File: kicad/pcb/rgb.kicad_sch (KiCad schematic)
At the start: 13 parts

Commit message: getting ready for prototype
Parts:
- removed JP1: Jumper_2_Open, Jumper:SolderJumper-2_P1.3mm_Open_TrianglePad1.0x1.5mm, symbol Jumper:Jumper_2_Open
- added JP2: SolderJumper_3_Open, Jumper:SolderJumper-3_P1.3mm_Open_RoundedPad1.0x1.5mm, symbol Jumper:SolderJumper_3_Open
- D101, D102, D103, D104, D105, D106, D107, D108, D109, D110, D111: footprint modified_footrprints:LED_SK6812MINI_PLCC4_3.5x3.5mm_P1.75mm -> modified_footprints:LED_SK6812MINI_PLCC4_3.5x3.5mm_P1.75mm
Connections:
- net RGB: now also JP2.2 (C)
- net at D111.3 (DIN), J?.2 (Pin_2): now also JP2.3 (B)
- net at D102.1 (DOUT), D103.3 (DIN): now also JP2.1 (A)
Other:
- title: Hotswap Chiffre -> Le Capybara
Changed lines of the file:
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@@
   (paper "A4")
   (title_block
-    (title "Hotswap Chiffre")
-    (date "2023-07-07")
-    (rev "0.2")
+    (title "Le Capybara")
+    (date "2023-08-22")
+    (rev "0.1")
     (company "sporkus")
   )
@@
   (junction (at 136.525 69.215) (diameter 0) (color 0 0 0 0)
   )
+  (junction (at 82.801 89.535) (diameter 0) (color 0 0 0 0)
+  )
   (junction (at 100.965 53.975) (diameter 0) (color 0 0 0 0)
   )
+  (junction (at 67.31 50.8) (diameter 0) (color 0 0 0 0)
+  )
   (junction (at 154.305 53.975) (diameter 0) (color 0 0 0 0)
   )
@@
   (junction (at 111.125 81.915) (diameter 0) (color 0 0 0 0)
   )
-  (junction (at 81.661 41.021) (diameter 0) (color 0 0 0 0)
-  )
   (junction (at 100.965 69.215) (diameter 0) (color 0 0 0 0)
   )
   (junction (at 118.745 53.975) (diameter 0) (color 0 0 0 0)
   )
+  (wire (pts (xy 64.77 50.8) (xy 67.31 50.8))
+    (stroke (width 0) (type default))
+  )
   (wire (pts (xy 78.105 84.455) (xy 78.105 86.995))
     (stroke (width 0) (type default))
@@
     (stroke (width 0) (type default))
   )
-  (wire (pts (xy 78.105 89.535) (xy 85.725 89.535))
+  (wire (pts (xy 78.105 89.535) (xy 82.801 89.535))
     (stroke (width 0) (type default))
   )
@@
     (stroke (width 0) (type default))
   )
+  (wire (pts (xy 82.801 89.535) (xy 85.725 89.535))
+    (stroke (width 0) (type default))
+  )
   (wire (pts (xy 146.685 97.155) (xy 164.465 97.155))
     (stroke (width 0) (type default))
   )
-  (wire (pts (xy 81.661 41.021) (xy 83.566 41.021))
-    (stroke (width 0) (type default))
-  )
   (wire (pts (xy 136.525 69.215) (xy 154.305 69.215))
     (stroke (width 0) (type default))
@@
     (stroke (width 0) (type default))
   )
-  (wire (pts (xy 81.661 41.021) (xy 81.661 61.595))
-    (stroke (width 0) (type default))
-  )
   (wire (pts (xy 93.345 97.155) (xy 111.125 97.155))
     (stroke (width 0) (type default))
   )
+  (wire (pts (xy 71.12 45.72) (xy 71.12 41.021))
+    (stroke (width 0) (type default))
+  )
+  (wire (pts (xy 71.12 68.58) (xy 82.801 68.58))
+    (stroke (width 0) (type default))
+  )
+  (wire (pts (xy 81.661 50.8) (xy 81.661 61.595))
+    (stroke (width 0) (type default))
+  )
   (wire (pts (xy 111.125 97.155) (xy 128.905 97.155))
     (stroke (width 0) (type default))
   )
-  (wire (pts (xy 71.755 41.021) (xy 81.661 41.021))
+  (wire (pts (xy 67.31 50.8) (xy 81.661 50.8))
     (stroke (width 0) (type default))
   )
@@
     (stroke (width 0) (type default))
   )
-  (wire (pts (xy 93.726 41.021) (xy 127.635 41.021))
+  (wire (pts (xy 71.12 55.88) (xy 71.12 68.58))
+    (stroke (width 0) (type default))
+  )
+  (wire (pts (xy 71.12 41.021) (xy 127.635 41.021))
+    (stroke (width 0) (type default))
+  )
+  (wire (pts (xy 82.801 68.58) (xy 82.801 89.535))
     (stroke (width 0) (type default))
   )
@@
     (stroke (width 0) (type default))
   )
-  (global_label "RGB" (shape input) (at 71.755 41.021 180)
+  (global_label "RGB" (shape input) (at 64.77 50.8 180)
     (effects (font (size 1.27 1.27)) (justify right))
-    (property "Intersheetrefs" "${INTERSHEET_REFS}" (at 71.755 41.021 0)
+    (property "Intersheetrefs" "${INTERSHEET_REFS}" (at 64.77 50.8 0)
       (effects (font (size 1.27 1.27)) hide)
     )
@@
       (effects (font (size 0.8 0.8)))
     )
-    (property "Footprint" "modified_footrprints:LED_SK6812MINI_PLCC4_3.5x3.5mm_P1.75mm" (at 147.955 97.155 0)
+    (property "Footprint" "modified_footprints:LED_SK6812MINI_PLCC4_3.5x3.5mm_P1.75mm" (at 147.955 97.155 0)
       (effects (font (size 1.27 1.27)) (justify left top) hide)
     )
@@
       (effects (font (size 0.8 0.8)))
     )
-    (property "Footprint" "modified_footrprints:LED_SK6812MINI_PLCC4_3.5x3.5mm_P1.75mm" (at 137.795 69.215 0)
+    (property "Footprint" "modified_footprints:LED_SK6812MINI_PLCC4_3.5x3.5mm_P1.75mm" (at 137.795 69.215 0)
       (effects (font (size 1.27 1.27)) (justify left top) hide)
     )
@@
         (path "/ca0d59d2-7f9b-4344-99bc-39bc2c8c88cb/ddb59433-fe5b-4efc-b099-e8e1feecfd95"
           (reference "D103") (unit 1)
+        )
+      )
+    )
+  )
+  (symbol (lib_id "Jumper:SolderJumper_3_Open") (at 71.12 50.8 270) (unit 1)
+    (in_bom yes) (on_board yes) (dnp no)
+    (property "Reference" "JP2" (at 73.66 53.34 90)
+      (effects (font (size 1.27 1.27)) (justify left))
+    )
+    (property "Value" "SolderJumper_3_Open" (at 46.99 57.15 90)
+      (effects (font (size 1.27 1.27)) (justify left) hide)
+    )
+    (property "Footprint" "Jumper:SolderJumper-3_P1.3mm_Open_RoundedPad1.0x1.5mm" (at 71.12 50.8 0)
+      (effects (font (size 1.27 1.27)) hide)
+    )
+    (property "Datasheet" "~" (at 71.12 50.8 0)
+      (effects (font (size 1.27 1.27)) hide)
+    )
+    (pin "1")
+    (pin "2")
+    (pin "3")
+    (instances
+      (project "le_capybara"
+        (path "/ca0d59d2-7f9b-4344-99bc-39bc2c8c88cb/ddb59433-fe5b-4efc-b099-e8e1feecfd95"
+          (reference "JP2") (unit 1)
         )
       )
@@
       (effects (font (size 0.8 0.8)))
     )
-    (property "Footprint" "modified_footrprints:LED_SK6812MINI_PLCC4_3.5x3.5mm_P1.75mm" (at 155.575 69.215 0)
+    (property "Footprint" "modified_footprints:LED_SK6812MINI_PLCC4_3.5x3.5mm_P1.75mm" (at 155.575 69.215 0)
       (effects (font (size 1.27 1.27)) (justify left top) hide)
     )
@@
       (effects (font (size 0.8 0.8)))
     )
-    (property "Footprint" "modified_footrprints:LED_SK6812MINI_PLCC4_3.5x3.5mm_P1.75mm" (at 94.615 97.155 0)
+    (property "Footprint" "modified_footprints:LED_SK6812MINI_PLCC4_3.5x3.5mm_P1.75mm" (at 94.615 97.155 0)
       (effects (font (size 1.27 1.27)) (justify left top) hide)
     )
@@
       (effects (font (size 0.8 0.8)))
     )
-    (property "Footprint" "modified_footrprints:LED_SK6812MINI_PLCC4_3.5x3.5mm_P1.75mm" (at 165.735 97.155 0)
+    (property "Footprint" "modified_footprints:LED_SK6812MINI_PLCC4_3.5x3.5mm_P1.75mm" (at 165.735 97.155 0)
       (effects (font (size 1.27 1.27)) (justify left top) hide)
     )
@@
       (effects (font (size 0.8 0.8)))
     )
-    (property "Footprint" "modified_footrprints:LED_SK6812MINI_PLCC4_3.5x3.5mm_P1.75mm" (at 112.395 97.155 0)
+    (property "Footprint" "modified_footprints:LED_SK6812MINI_PLCC4_3.5x3.5mm_P1.75mm" (at 112.395 97.155 0)
       (effects (font (size 1.27 1.27)) (justify left top) hide)
     )
@@
       (effects (font (size 0.8 0.8)))
     )
-    (property "Footprint" "modified_footrprints:LED_SK6812MINI_PLCC4_3.5x3.5mm_P1.75mm" (at 120.015 69.215 0)
+    (property "Footprint" "modified_footprints:LED_SK6812MINI_PLCC4_3.5x3.5mm_P1.75mm" (at 120.015 69.215 0)
       (effects (font (size 1.27 1.27)) (justify left top) hide)
     )
@@
       (effects (font (size 0.8 0.8)))
     )
-    (property "Footprint" "modified_footrprints:LED_SK6812MINI_PLCC4_3.5x3.5mm_P1.75mm" (at 183.515 97.155 0)
+    (property "Footprint" "modified_footprints:LED_SK6812MINI_PLCC4_3.5x3.5mm_P1.75mm" (at 183.515 97.155 0)
       (effects (font (size 1.27 1.27)) (justify left top) hide)
     )
@@
       (effects (font (size 0.8 0.8)))
     )
-    (property "Footprint" "modified_footrprints:LED_SK6812MINI_PLCC4_3.5x3.5mm_P1.75mm" (at 102.235 69.215 0)
+    (property "Footprint" "modified_footprints:LED_SK6812MINI_PLCC4_3.5x3.5mm_P1.75mm" (at 102.235 69.215 0)
       (effects (font (size 1.27 1.27)) (justify left top) hide)
     )
@@
       (effects (font (size 0.8 0.8)))
     )
-    (property "Footprint" "modified_footrprints:LED_SK6812MINI_PLCC4_3.5x3.5mm_P1.75mm" (at 173.355 69.215 0)
+    (property "Footprint" "modified_footprints:LED_SK6812MINI_PLCC4_3.5x3.5mm_P1.75mm" (at 173.355 69.215 0)
       (effects (font (size 1.27 1.27)) (justify left top) hide)
     )
@@
       (effects (font (size 0.8 0.8)))
     )
-    (property "Footprint" "modified_footrprints:LED_SK6812MINI_PLCC4_3.5x3.5mm_P1.75mm" (at 130.175 97.155 0)
+    (property "Footprint" "modified_footprints:LED_SK6812MINI_PLCC4_3.5x3.5mm_P1.75mm" (at 130.175 97.155 0)
       (effects (font (size 1.27 1.27)) (justify left top) hide)
     )
@@
         )
       )
-    )
-  )
-  (symbol (lib_id "Jumper:Jumper_2_Open") (at 88.646 41.021 0) (unit 1)
-    (in_bom yes) (on_board yes) (dnp no) (fields_autoplaced)
-    (property "Reference" "JP1" (at 88.646 34.29 0)
-      (effects (font (size 1.27 1.27)))
-    )
-    (property "Value" "Jumper_2_Open" (at 88.646 36.83 0)
-      (effects (font (size 1.27 1.27)))
-    )
-    (property "Footprint" "Jumper:SolderJumper-2_P1.3mm_Open_TrianglePad1.0x1.5mm" (at 88.646 41.021 0)
-      (effects (font (size 1.27 1.27)) hide)
-    )
-    (property "Datasheet" "~" (at 88.646 41.021 0)
-      (effects (font (size 1.27 1.27)) hide)
-    )
-    (pin "1")
-    (pin "2")
-    (instances
-      (project "le_capybara"
-        (path "/ca0d59d2-7f9b-4344-99bc-39bc2c8c88cb/ddb59433-fe5b-4efc-b099-e8e1feecfd95"
-          (reference "JP1") (unit 1)
-        )
-      )

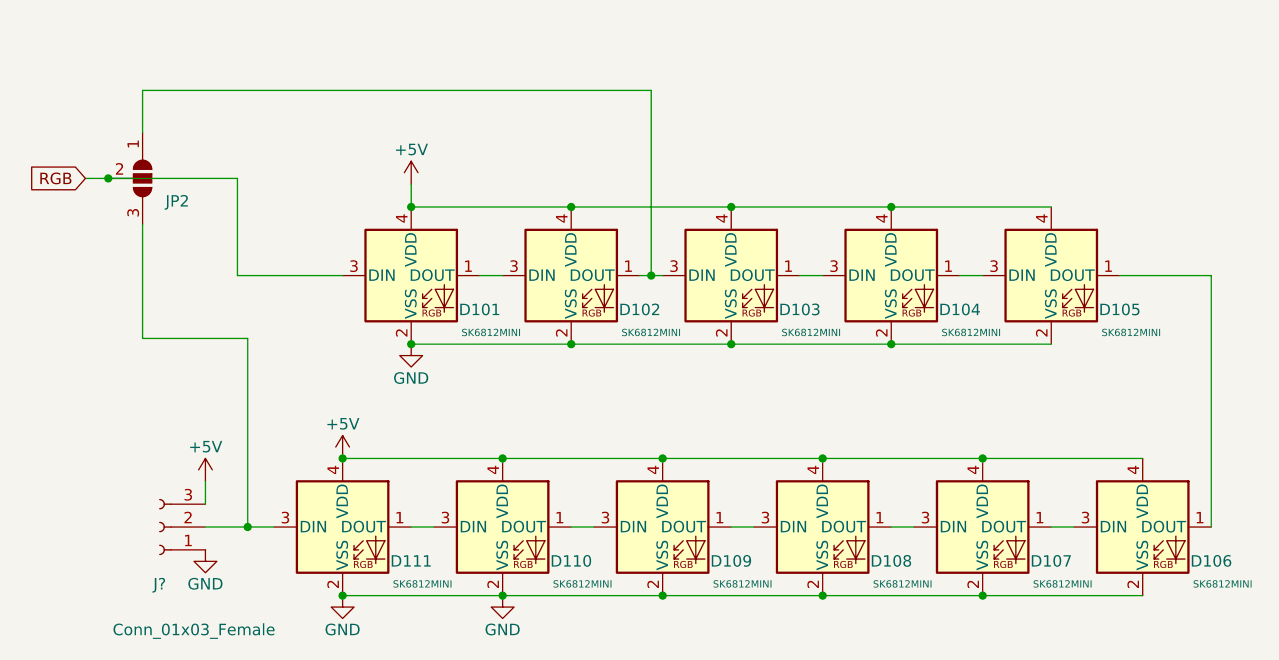
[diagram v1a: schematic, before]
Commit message: Major fixes after prototype order
Fixed the following:
- wrong RGB schematic, D106-D111 doesn't work
- discharge pin from analog circuit was not connected
- plate holes had the wrong diameter
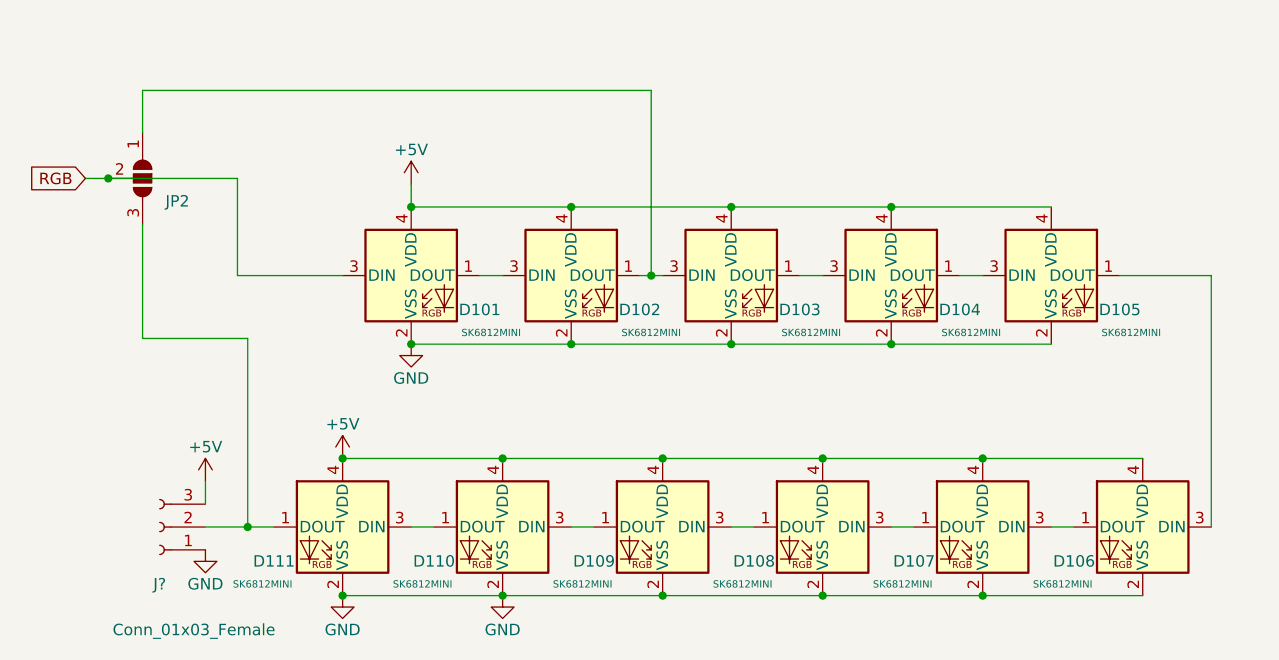
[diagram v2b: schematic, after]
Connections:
- net at J?.2 (Pin_2), JP2.3 (B): now also D111.1 (DOUT); no longer D111.3 (DIN)
- net at D108.1 (DOUT): now also D109.3 (DIN); no longer D107.3 (DIN)
- net at D108.3 (DIN): now also D107.1 (DOUT); no longer D109.1 (DOUT)
- net at D110.3 (DIN): now also D109.1 (DOUT); no longer D111.1 (DOUT)
- net at D106.3 (DIN): now also D105.1 (DOUT); no longer D107.1 (DOUT)
- net at D110.1 (DOUT): now also D111.3 (DIN); no longer D109.3 (DIN)
- net at D106.1 (DOUT): now also D107.3 (DIN); no longer D105.1 (DOUT)
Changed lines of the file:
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@@
   (title_block
     (title "Le Capybara")
-    (date "2023-08-22")
-    (rev "0.1")
+    (date "2023-09-01")
+    (rev "0.2")
     (company "sporkus")
   )
@@
     )
   )
-  (symbol (lib_id "LED:SK6812MINI") (at 146.685 89.535 0) (unit 1)
-    (in_bom yes) (on_board yes) (dnp no)
-    (property "Reference" "D108" (at 154.305 93.345 0)
-      (effects (font (size 1.27 1.27)))
-    )
-    (property "Value" "SK6812MINI" (at 155.575 95.885 0)
-      (effects (font (size 0.8 0.8)))
-    )
-    (property "Footprint" "modified_footprints:LED_SK6812MINI_PLCC4_3.5x3.5mm_P1.75mm" (at 147.955 97.155 0)
-      (effects (font (size 1.27 1.27)) (justify left top) hide)
-    )
-    (property "Datasheet" "https://cdn-shop.adafruit.com/product-files/2686/SK6812MINI_REV.01-1-2.pdf" (at 149.225 99.06 0)
+  (symbol (lib_id "LED:SK6812MINI") (at 146.685 89.535 0) (mirror y) (unit 1)
+    (in_bom yes) (on_board yes) (dnp no)
+    (property "Reference" "D108" (at 139.065 93.345 0)
+      (effects (font (size 1.27 1.27)))
+    )
+    (property "Value" "SK6812MINI" (at 137.795 95.885 0)
+      (effects (font (size 0.8 0.8)))
+    )
+    (property "Footprint" "modified_footprints:LED_SK6812MINI_PLCC4_3.5x3.5mm_P1.75mm" (at 145.415 97.155 0)
+      (effects (font (size 1.27 1.27)) (justify left top) hide)
+    )
+    (property "Datasheet" "https://cdn-shop.adafruit.com/product-files/2686/SK6812MINI_REV.01-1-2.pdf" (at 144.145 99.06 0)
       (effects (font (size 1.27 1.27)) (justify left top) hide)
     )
@@
     )
   )
-  (symbol (lib_id "LED:SK6812MINI") (at 93.345 89.535 0) (unit 1)
-    (in_bom yes) (on_board yes) (dnp no)
-    (property "Reference" "D111" (at 100.965 93.345 0)
-      (effects (font (size 1.27 1.27)))
-    )
-    (property "Value" "SK6812MINI" (at 102.235 95.885 0)
-      (effects (font (size 0.8 0.8)))
-    )
-    (property "Footprint" "modified_footprints:LED_SK6812MINI_PLCC4_3.5x3.5mm_P1.75mm" (at 94.615 97.155 0)
-      (effects (font (size 1.27 1.27)) (justify left top) hide)
-    )
-    (property "Datasheet" "https://cdn-shop.adafruit.com/product-files/2686/SK6812MINI_REV.01-1-2.pdf" (at 95.885 99.06 0)
+  (symbol (lib_id "LED:SK6812MINI") (at 93.345 89.535 0) (mirror y) (unit 1)
+    (in_bom yes) (on_board yes) (dnp no)
+    (property "Reference" "D111" (at 85.725 93.345 0)
+      (effects (font (size 1.27 1.27)))
+    )
+    (property "Value" "SK6812MINI" (at 84.455 95.885 0)
+      (effects (font (size 0.8 0.8)))
+    )
+    (property "Footprint" "modified_footprints:LED_SK6812MINI_PLCC4_3.5x3.5mm_P1.75mm" (at 92.075 97.155 0)
+      (effects (font (size 1.27 1.27)) (justify left top) hide)
+    )
+    (property "Datasheet" "https://cdn-shop.adafruit.com/product-files/2686/SK6812MINI_REV.01-1-2.pdf" (at 90.805 99.06 0)
       (effects (font (size 1.27 1.27)) (justify left top) hide)
     )
@@
     )
   )
-  (symbol (lib_id "LED:SK6812MINI") (at 164.465 89.535 0) (unit 1)
-    (in_bom yes) (on_board yes) (dnp no)
-    (property "Reference" "D107" (at 172.085 93.345 0)
-      (effects (font (size 1.27 1.27)))
-    )
-    (property "Value" "SK6812MINI" (at 173.355 95.885 0)
-      (effects (font (size 0.8 0.8)))
-    )
-    (property "Footprint" "modified_footprints:LED_SK6812MINI_PLCC4_3.5x3.5mm_P1.75mm" (at 165.735 97.155 0)
-      (effects (font (size 1.27 1.27)) (justify left top) hide)
-    )
-    (property "Datasheet" "https://cdn-shop.adafruit.com/product-files/2686/SK6812MINI_REV.01-1-2.pdf" (at 167.005 99.06 0)
+  (symbol (lib_id "LED:SK6812MINI") (at 164.465 89.535 0) (mirror y) (unit 1)
+    (in_bom yes) (on_board yes) (dnp no)
+    (property "Reference" "D107" (at 156.845 93.345 0)
+      (effects (font (size 1.27 1.27)))
+    )
+    (property "Value" "SK6812MINI" (at 155.575 95.885 0)
+      (effects (font (size 0.8 0.8)))
+    )
+    (property "Footprint" "modified_footprints:LED_SK6812MINI_PLCC4_3.5x3.5mm_P1.75mm" (at 163.195 97.155 0)
+      (effects (font (size 1.27 1.27)) (justify left top) hide)
+    )
+    (property "Datasheet" "https://cdn-shop.adafruit.com/product-files/2686/SK6812MINI_REV.01-1-2.pdf" (at 161.925 99.06 0)
       (effects (font (size 1.27 1.27)) (justify left top) hide)
     )
@@
     )
   )
-  (symbol (lib_id "LED:SK6812MINI") (at 111.125 89.535 0) (unit 1)
-    (in_bom yes) (on_board yes) (dnp no)
-    (property "Reference" "D110" (at 118.745 93.345 0)
-      (effects (font (size 1.27 1.27)))
-    )
-    (property "Value" "SK6812MINI" (at 120.015 95.885 0)
-      (effects (font (size 0.8 0.8)))
-    )
-    (property "Footprint" "modified_footprints:LED_SK6812MINI_PLCC4_3.5x3.5mm_P1.75mm" (at 112.395 97.155 0)
-      (effects (font (size 1.27 1.27)) (justify left top) hide)
-    )
-    (property "Datasheet" "https://cdn-shop.adafruit.com/product-files/2686/SK6812MINI_REV.01-1-2.pdf" (at 113.665 99.06 0)
+  (symbol (lib_id "LED:SK6812MINI") (at 111.125 89.535 0) (mirror y) (unit 1)
+    (in_bom yes) (on_board yes) (dnp no)
+    (property "Reference" "D110" (at 103.505 93.345 0)
+      (effects (font (size 1.27 1.27)))
+    )
+    (property "Value" "SK6812MINI" (at 102.235 95.885 0)
+      (effects (font (size 0.8 0.8)))
+    )
+    (property "Footprint" "modified_footprints:LED_SK6812MINI_PLCC4_3.5x3.5mm_P1.75mm" (at 109.855 97.155 0)
+      (effects (font (size 1.27 1.27)) (justify left top) hide)
+    )
+    (property "Datasheet" "https://cdn-shop.adafruit.com/product-files/2686/SK6812MINI_REV.01-1-2.pdf" (at 108.585 99.06 0)
       (effects (font (size 1.27 1.27)) (justify left top) hide)
     )
@@
     )
   )
-  (symbol (lib_id "LED:SK6812MINI") (at 182.245 89.535 0) (unit 1)
-    (in_bom yes) (on_board yes) (dnp no)
-    (property "Reference" "D106" (at 189.865 93.345 0)
-      (effects (font (size 1.27 1.27)))
-    )
-    (property "Value" "SK6812MINI" (at 191.135 95.885 0)
-      (effects (font (size 0.8 0.8)))
-    )
-    (property "Footprint" "modified_footprints:LED_SK6812MINI_PLCC4_3.5x3.5mm_P1.75mm" (at 183.515 97.155 0)
-      (effects (font (size 1.27 1.27)) (justify left top) hide)
-    )
-    (property "Datasheet" "https://cdn-shop.adafruit.com/product-files/2686/SK6812MINI_REV.01-1-2.pdf" (at 184.785 99.06 0)
+  (symbol (lib_id "LED:SK6812MINI") (at 182.245 89.535 0) (mirror y) (unit 1)
+    (in_bom yes) (on_board yes) (dnp no)
+    (property "Reference" "D106" (at 174.625 93.345 0)
+      (effects (font (size 1.27 1.27)))
+    )
+    (property "Value" "SK6812MINI" (at 173.355 95.885 0)
+      (effects (font (size 0.8 0.8)))
+    )
+    (property "Footprint" "modified_footprints:LED_SK6812MINI_PLCC4_3.5x3.5mm_P1.75mm" (at 180.975 97.155 0)
+      (effects (font (size 1.27 1.27)) (justify left top) hide)
+    )
+    (property "Datasheet" "https://cdn-shop.adafruit.com/product-files/2686/SK6812MINI_REV.01-1-2.pdf" (at 179.705 99.06 0)
       (effects (font (size 1.27 1.27)) (justify left top) hide)
     )
@@
     )
   )
-  (symbol (lib_id "LED:SK6812MINI") (at 128.905 89.535 0) (unit 1)
-    (in_bom yes) (on_board yes) (dnp no)
-    (property "Reference" "D109" (at 136.525 93.345 0)
-      (effects (font (size 1.27 1.27)))
-    )
-    (property "Value" "SK6812MINI" (at 137.795 95.885 0)
-      (effects (font (size 0.8 0.8)))
-    )
-    (property "Footprint" "modified_footprints:LED_SK6812MINI_PLCC4_3.5x3.5mm_P1.75mm" (at 130.175 97.155 0)
-      (effects (font (size 1.27 1.27)) (justify left top) hide)
-    )
-    (property "Datasheet" "https://cdn-shop.adafruit.com/product-files/2686/SK6812MINI_REV.01-1-2.pdf" (at 131.445 99.06 0)
-      (effects (font (size 1.27 1.27)) (justify left top) hide)
-    )
+  (symbol (lib_id "LED:SK6812MINI") (at 128.905 89.535 0) (mirror y) (unit 1)
+    (in_bom yes) (on_board yes) (dnp no)
+    (property "Reference" "D109" (at 121.285 93.345 0)
+      (effects (font (size 1.27 1.27)))
+    )
+    (property "Value" "SK6812MINI" (at 120.015 95.885 0)
+      (effects (font (size 0.8 0.8)))
+    )
+    (property "Footprint" "modified_footprints:LED_SK6812MINI_PLCC4_3.5x3.5mm_P1.75mm" (at 127.635 97.155 0)
+      (effects (font (size 1.27 1.27)) (justify left top) hide)
+    )
+    (property "Datasheet" "https://cdn-shop.adafruit.com/product-files/2686/SK6812MINI_REV.01-1-2.pdf" (at 126.365 99.06 0)
+      (effects (font (size 1.27 1.27)) (justify left top) hide)
+    )
